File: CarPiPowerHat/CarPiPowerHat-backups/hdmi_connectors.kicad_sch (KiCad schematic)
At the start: 2 parts, among them J1 HDMI_A_1.4, J6 1-84953-5

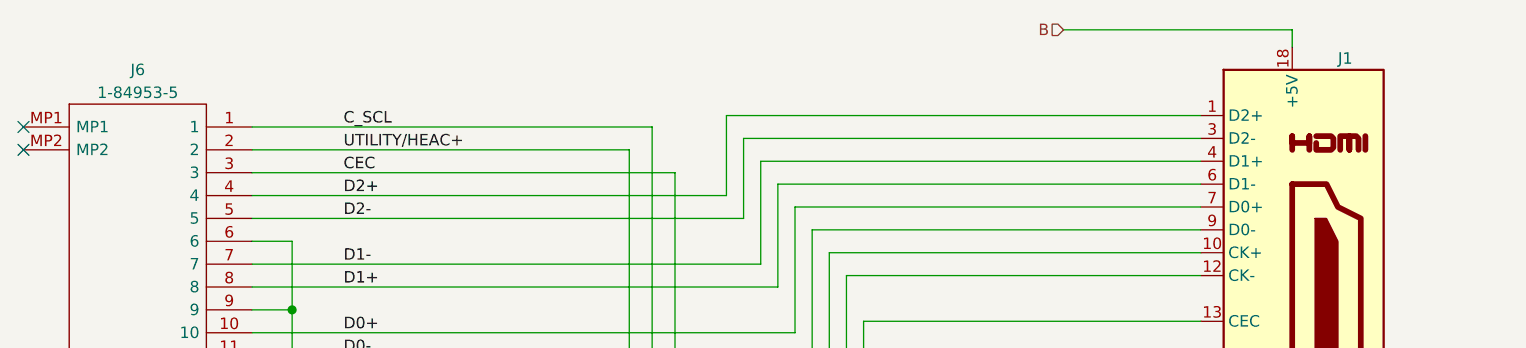
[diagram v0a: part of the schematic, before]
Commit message: Repositioning of connectors
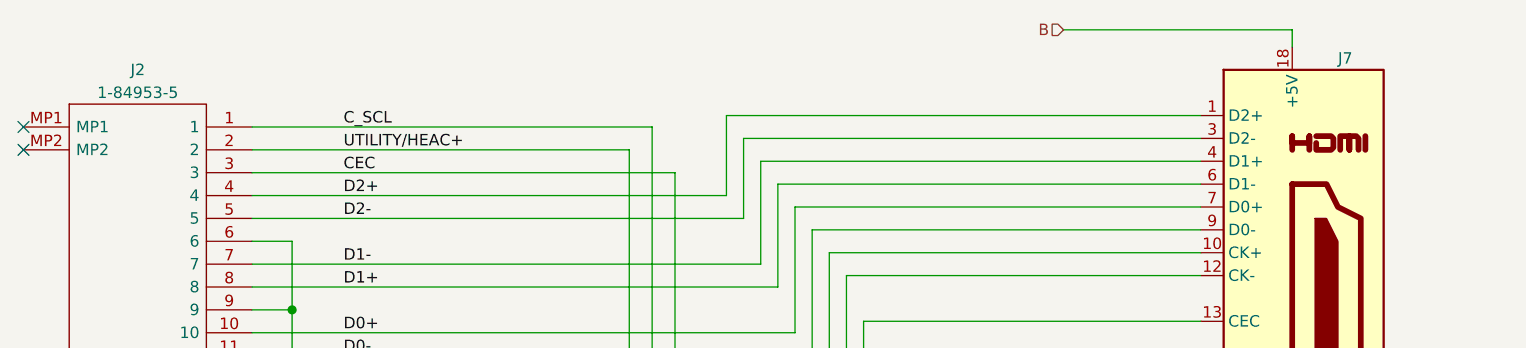
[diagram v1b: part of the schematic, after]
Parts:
- renumbered J6 to J2, J1 to J7
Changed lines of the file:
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@@
   (symbol (lib_id "power:GND") (at 75.565 77.47 0)
     (in_bom yes) (on_board yes)
-    (property "Reference" "#PWR0130" (id 0) (at 75.565 83.82 0)
+    (property "Reference" "#PWR0133" (id 0) (at 75.565 83.82 0)
       (effects (font (size 1.27 1.27)) hide)
     )
@@
   (symbol (lib_id "power:GND") (at 181.61 80.645 0)
     (in_bom yes) (on_board yes)
-    (property "Reference" "#PWR0106" (id 0) (at 181.61 86.995 0)
+    (property "Reference" "#PWR0134" (id 0) (at 181.61 86.995 0)
       (effects (font (size 1.27 1.27)) hide)
     )
@@
   (symbol (lib_id "power:GND") (at 202.565 80.645 0)
     (in_bom yes) (on_board yes)
-    (property "Reference" "#PWR0131" (id 0) (at 202.565 86.995 0)
+    (property "Reference" "#PWR0135" (id 0) (at 202.565 86.995 0)
       (effects (font (size 1.27 1.27)) hide)
     )
@@
   (symbol (lib_id "power:GND") (at 218.44 90.805 0)
     (in_bom yes) (on_board yes)
-    (property "Reference" "#PWR0132" (id 0) (at 218.44 97.155 0)
+    (property "Reference" "#PWR0136" (id 0) (at 218.44 97.155 0)
       (effects (font (size 1.27 1.27)) hide)
     )
@@
   (symbol (lib_id "1-84953-5:1-84953-5") (at 45.72 30.48 0)
     (in_bom yes) (on_board yes)
-    (property "Reference" "J6" (id 0) (at 58.42 24.13 0))
+    (property "Reference" "J2" (id 0) (at 58.42 24.13 0))
     (property "Value" "1-84953-5" (id 1) (at 58.42 26.67 0))
     (property "Footprint" "project_footprints:1849535" (id 2) (at 67.31 27.94 0)
@@
   (symbol (lib_id "CarPiPowerHat:HDMI_A_1.4") (at 186.69 49.53 0)
     (in_bom yes) (on_board yes)
-    (property "Reference" "J1" (id 0) (at 191.77 22.86 0)
+    (property "Reference" "J7" (id 0) (at 191.77 22.86 0)
       (effects (font (size 1.27 1.27)) (justify left))
     )
